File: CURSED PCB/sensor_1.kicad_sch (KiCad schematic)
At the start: 20 parts, among them J1 Programming Header, J2 Micro_SD_Card, J4 2 Wire Block for PZT, U10 MCP2562, U12 AD5761BRUZ, U3 STM32G431KBT6, Y1 24Hz crystal

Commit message: i am a LED
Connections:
- net +3.3VD: no longer JP2.2 (B)
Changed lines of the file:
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@@
-	)
-	(junction
-		(at 34.29 20.32)
-		(diameter 0)
-		(color 0 0 0 0)
 	)
 	(junction
@@
 	(wire
 		(pts
-			(xy 34.29 20.32) (xy 34.29 19.05)
-		)
-		(stroke
-			(width 0)
-			(type default)
-		)
-	)
-	(wire
-		(pts
 			(xy 66.04 74.93) (xy 85.09 74.93)
 		)
@@
 	(wire
 		(pts
-			(xy 34.29 20.32) (xy 34.29 36.83)
+			(xy 34.29 19.05) (xy 34.29 36.83)
 		)
 		(stroke
@@
 	(wire
 		(pts
-			(xy 34.29 20.32) (xy 38.1 20.32)
-		)
-		(stroke
-			(width 0)
-			(type default)
-		)
-	)
-	(wire
-		(pts
 			(xy 118.11 121.92) (xy 118.11 129.54)
 		)
@@
 		)
 		(stroke
-			(width 0)
-			(type default)
-		)
-	)
-	(wire
-		(pts
-			(xy 38.1 20.32) (xy 38.1 25.4)
-		)
-		(stroke

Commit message: tee
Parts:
- added D1: RED LED, LED_SMD:LED_0603_1608Metric_Pad1.05x0.95mm_HandSolder, symbol Device:LED
- added D3: GREEN LED, LED_SMD:LED_0603_1608Metric_Pad1.05x0.95mm_HandSolder, symbol Device:LED
- added R1, R3, R4, R5: 22R, Resistor_SMD:R_0603_1608Metric_Pad0.98x0.95mm_HandSolder, symbol Device:R_US
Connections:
- net +3.3VD: now also JP2.2 (B); no longer D2.1 (K), R2.1
- net MISO: now also R5.1; no longer J2.7 (DAT0)
- net MOSI: now also R4.1; no longer J2.3 (CMD)
- net at D2.2 (A), JP2.1 (A): now also D1.2 (A), D3.2 (A)
- net at U3.5 (PA0): now also R3.2
- net at U3.7 (PA2): now also R1.2
- new net: J2.3 (CMD), R4.2
- new net: D3.1 (K), R3.1
- new net: D1.1 (K), R1.1
- new net: D2.1 (K), R2.1
- new net: J2.7 (DAT0), R5.2
- no-connect marks 12 -> 10
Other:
- moved on the sheet: D2, JP2, R2

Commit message: wire
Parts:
- added R14: 22R, Resistor_SMD:R_0603_1608Metric_Pad0.98x0.95mm_HandSolder, symbol Device:R_US
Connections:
- net CS2: now also R14.1; no longer J2.2 (DAT3/CD)
- net MKLKIN: now also U3.21 (PA11)
- new net: J2.2 (DAT3/CD), R14.2
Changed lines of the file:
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@@
 	(wire
 		(pts
+			(xy 71.12 67.31) (xy 85.09 67.31)
+		)
+		(stroke
+			(width 0)
+			(type default)
+		)
+	)
+	(wire
+		(pts
 			(xy 30.48 25.4) (xy 46.99 25.4)
 		)
@@
 	(wire
 		(pts
-			(xy 13.97 157.48) (xy 62.23 157.48)
+			(xy 25.4 149.86) (xy 15.24 149.86)
 		)
 		(stroke
@@
 	(wire
 		(pts
+			(xy 15.24 157.48) (xy 62.23 157.48)
+		)
+		(stroke
+			(width 0)
+			(type default)
+		)
+	)
+	(wire
+		(pts
 			(xy 52.07 167.64) (xy 52.07 185.42)
 		)
@@
 	)
 	(label "MKLKIN"
-		(at 63.5 66.04 0)
+		(at 71.12 67.31 0)
 		(effects
 			(font
@@
 	)
 	(label "CS2"
-		(at 13.97 157.48 0)
+		(at 25.4 149.86 0)
 		(effects
 			(font
@@
 					(unit 1)
 				)
+			)
+		)
+	)
+	(symbol
+		(lib_id "Device:R_US")
+		(at 15.24 153.67 0)
+		(unit 1)
+		(exclude_from_sim no)
+		(in_bom yes)
+		(on_board yes)
+		(dnp no)
+		(fields_autoplaced yes)
+		(property "Reference" "R14"
+			(at 17.78 152.3999 0)
+			(effects
+				(font
+					(size 1.27 1.27)
+				)
+				(justify left)
+			)
+		)
+		(property "Value" "22R"
+			(at 17.78 154.9399 0)
+			(effects
+				(font
+					(size 1.27 1.27)
+				)
+				(justify left)
+			)
+		)
+		(property "Footprint" "Resistor_SMD:R_0603_1608Metric_Pad0.98x0.95mm_HandSolder"
+			(at 16.256 153.924 90)
+			(effects
+				(font
+					(size 1.27 1.27)
+				)
+				(hide yes)
+			)
+		)
+		(property "Datasheet" "~"
+			(at 15.24 153.67 0)
+			(effects
+				(font
+					(size 1.27 1.27)
+				)
+				(hide yes)
+			)
+		)
+		(property "Description" "Resistor, US symbol"
+			(at 15.24 153.67 0)
+			(effects
+				(font
+					(size 1.27 1.27)
+				)
+				(hide yes)
+			)
+		)
+		(pin "2"
+		)
+		(pin "1"
+		)
+		(instances
+			(project "sensor_1"
+				(path "/9fb1a86f-679c-4b88-9ed1-932f4f414580"
+					(reference "R14")
+					(unit 1)
+				)

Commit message: small error
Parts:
- R1, R2, R3: value 22R -> 220R
- R14, R4, R5: value 22R -> 10k
- Y1: value 24Hz crystal -> 24MHz crystal
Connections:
- no-connect marks 10 -> 12
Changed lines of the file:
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@@
 	)
 	(no_connect
+		(at 85.09 69.85)
+	)
+	(no_connect
+		(at 85.09 59.69)
+	)
+	(no_connect
 		(at 138.43 91.44)
 	)
@@
 			)
 		)
-		(property "Value" "22R"
+		(property "Value" "10k"
 			(at 27.94 157.4799 0)
 			(effects
@@
 			)
 		)
-		(property "Value" "22R"
+		(property "Value" "220R"
 			(at 49.53 39.3699 0)
 			(effects
@@
 			)
 		)
-		(property "Value" "22R"
+		(property "Value" "220R"
 			(at 33.02 43.1799 0)
 			(effects
@@
 			)
 		)
-		(property "Value" "24Hz crystal"
+		(property "Value" "24MHz crystal"
 			(at 218.44 138.3598 90)
 			(effects
@@
 			)
 		)
-		(property "Value" "22R"
+		(property "Value" "10k"
 			(at 46.99 173.9899 0)
 			(effects
@@
 			)
 		)
-		(property "Value" "22R"
+		(property "Value" "220R"
 			(at 17.78 44.4499 0)
 			(effects
@@
 			)
 		)
-		(property "Value" "22R"
+		(property "Value" "10k"
 			(at 17.78 154.9399 0)
 			(effects

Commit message: redone pcb
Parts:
- removed J1: Programming Header, canhw_footprints:PinSocket_5x2.54_SMD_90deg_952-3198-1-ND, symbol Connector:Conn_01x05_Socket
- added J1: Conn_02x07_Odd_Even, Connector_PinHeader_1.27mm:PinHeader_2x07_P1.27mm_Vertical_SMD, symbol Connector_Generic:Conn_02x07_Odd_Even
- C1, C2, C3, C4, C5, C6, C7: footprint Capacitor_SMD:C_0603_1608Metric_Pad1.08x0.95mm_HandSolder -> Capacitor_SMD:C_0805_2012Metric_Pad1.18x1.45mm_HandSolder
- D1, D2, D3: footprint LED_SMD:LED_0603_1608Metric_Pad1.05x0.95mm_HandSolder -> LED_SMD:LED_0805_2012Metric_Pad1.15x1.40mm_HandSolder
- R1, R14, R2, R3, R4, R5: footprint Resistor_SMD:R_0603_1608Metric_Pad0.98x0.95mm_HandSolder -> Resistor_SMD:R_0805_2012Metric_Pad1.20x1.40mm_HandSolder
- TP1, TP4, TP5: footprint TestPoint:TestPoint_Loop_D2.50mm_Drill1.0mm -> TestPoint:TestPoint_Pad_1.5x1.5mm
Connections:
- net +3.3VD: now also R14.1, R4.1, R5.1, J1.8 (Pin_8)
- net CS2: now also J2.2 (DAT3/CD), R14.2; no longer R14.1
- net GND: now also J1.10 (Pin_10); no longer C3.1, C7.2, U3.14 (VSSA)
- net MCLR: now also J1.12 (Pin_12)
- net MISO: now also J2.7 (DAT0), R5.2; no longer R5.1
- net MOSI: now also J2.3 (CMD), R4.2; no longer R4.1
- net PGC/ICSPDAT: now also J1.4 (Pin_4)
- net PGD/ICSPCLK: now also J1.6 (Pin_6)
- new net AGND: C3.1, C7.2, U3.14 (VSSA)
- no-connect marks 12 -> 21
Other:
- moved on the sheet: C1, R4, R5

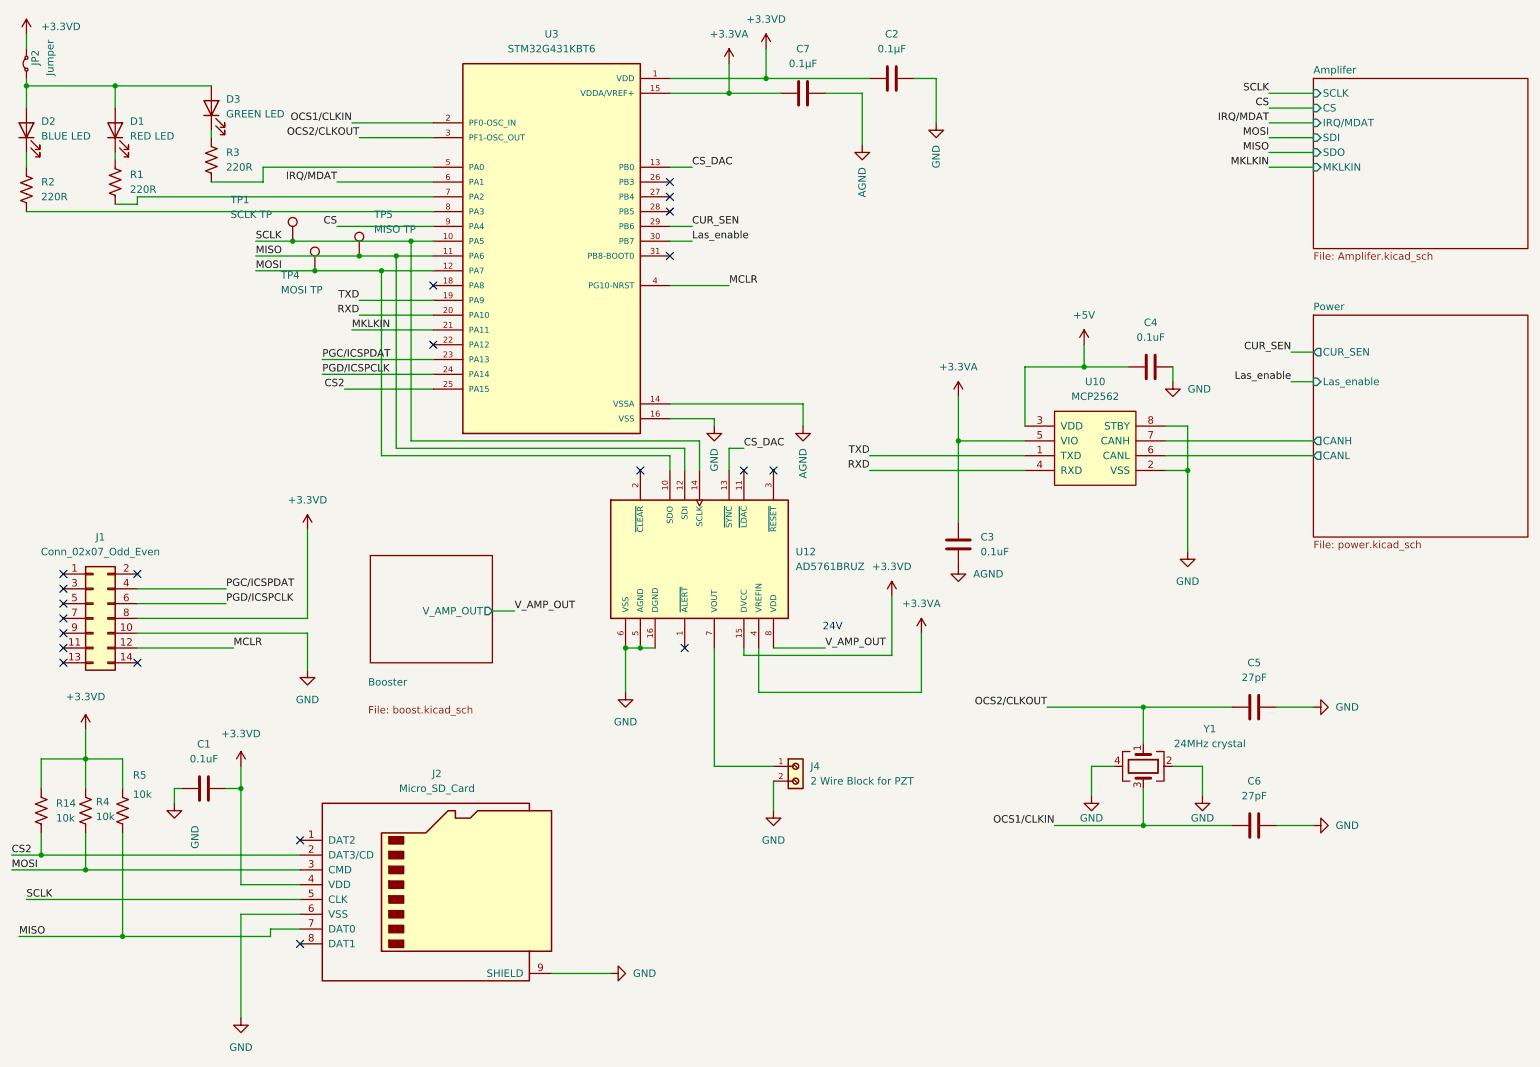
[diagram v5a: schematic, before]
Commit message: no spilt-ground plane (bad idea)
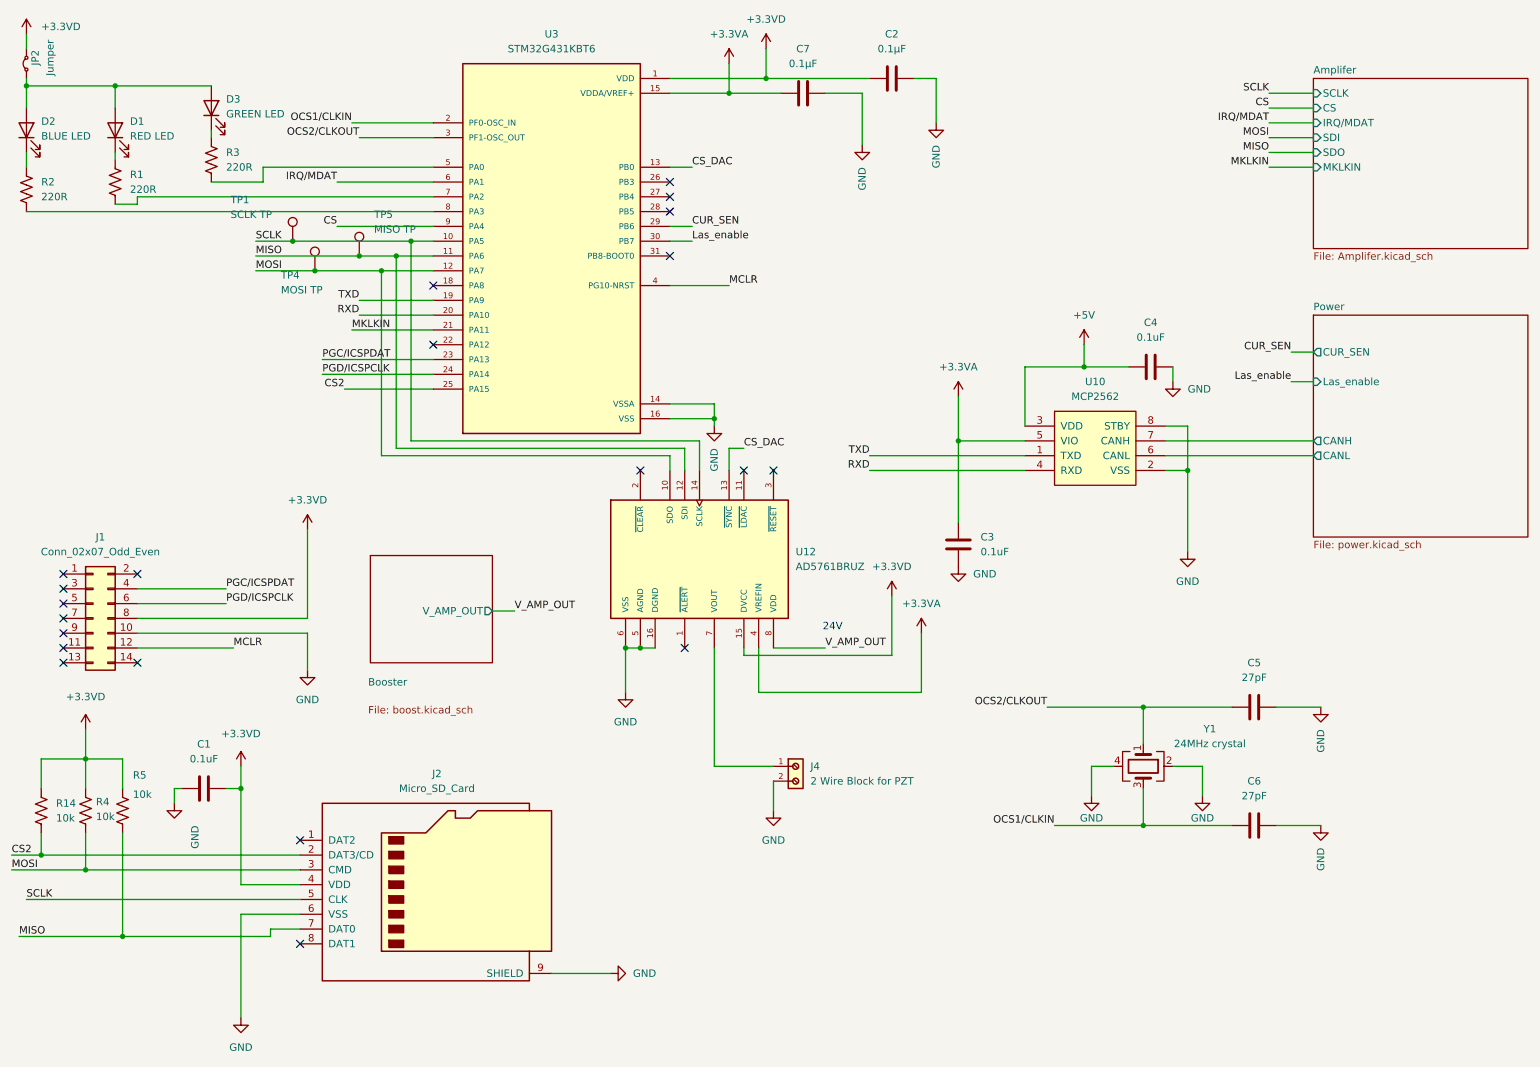
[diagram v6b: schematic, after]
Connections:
- net AGND is gone; now on net GND: C3.1, C7.2, U3.14 (VSSA)
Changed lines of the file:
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@@
 	)
 	(junction
+		(at 133.35 82.55)
+		(diameter 0)
+		(color 0 0 0 0)
+	)
+	(junction
 		(at 76.2 57.15)
 		(diameter 0)
@@
 	(wire
 		(pts
-			(xy 229.87 152.4) (xy 236.22 152.4)
+			(xy 229.87 152.4) (xy 237.49 152.4)
 		)
 		(stroke
@@
 	(wire
 		(pts
-			(xy 148.59 80.01) (xy 148.59 83.82)
+			(xy 142.24 24.13) (xy 160.02 24.13)
 		)
 		(stroke
@@
 	(wire
 		(pts
-			(xy 142.24 24.13) (xy 160.02 24.13)
+			(xy 71.12 31.75) (xy 85.09 31.75)
 		)
 		(stroke
@@
 	(wire
 		(pts
-			(xy 71.12 31.75) (xy 85.09 31.75)
+			(xy 31.75 171.45) (xy 57.15 171.45)
 		)
 		(stroke
@@
 	(wire
 		(pts
-			(xy 31.75 171.45) (xy 57.15 171.45)
+			(xy 46.99 41.91) (xy 55.88 41.91)
 		)
 		(stroke
@@
 	(wire
 		(pts
-			(xy 46.99 41.91) (xy 55.88 41.91)
+			(xy 229.87 132.08) (xy 237.49 132.08)
 		)
 		(stroke
@@
 	(wire
 		(pts
-			(xy 125.73 80.01) (xy 148.59 80.01)
-		)
-		(stroke
-			(width 0)
-			(type default)
-		)
-	)
-	(wire
-		(pts
 			(xy 15.24 24.13) (xy 15.24 25.4)
 		)
@@
 	(wire
 		(pts
-			(xy 229.87 132.08) (xy 236.22 132.08)
+			(xy 52.07 142.24) (xy 52.07 146.05)
 		)
 		(stroke
@@
 	(wire
 		(pts
-			(xy 52.07 142.24) (xy 52.07 146.05)
+			(xy 160.02 88.9) (xy 186.69 88.9)
 		)
 		(stroke
@@
 	(wire
 		(pts
-			(xy 160.02 88.9) (xy 186.69 88.9)
+			(xy 214.63 83.82) (xy 214.63 91.44)
 		)
 		(stroke
@@
 	(wire
 		(pts
-			(xy 214.63 83.82) (xy 214.63 91.44)
+			(xy 72.39 34.29) (xy 85.09 34.29)
 		)
 		(stroke
@@
 	(wire
 		(pts
-			(xy 72.39 34.29) (xy 85.09 34.29)
+			(xy 55.88 39.37) (xy 85.09 39.37)
 		)
 		(stroke
@@
 	(wire
 		(pts
-			(xy 55.88 39.37) (xy 85.09 39.37)
+			(xy 138.43 121.92) (xy 138.43 123.19)
 		)
 		(stroke
@@
 	(wire
 		(pts
-			(xy 138.43 121.92) (xy 138.43 123.19)
+			(xy 133.35 80.01) (xy 133.35 82.55)
 		)
 		(stroke
@@
 	(wire
 		(pts
+			(xy 125.73 80.01) (xy 133.35 80.01)
+		)
+		(stroke
+			(width 0)
+			(type default)
+		)
+	)
+	(wire
+		(pts
 			(xy 72.39 64.77) (xy 85.09 64.77)
 		)
@@
 	)
 	(symbol
-		(lib_id "power:GND")
-		(at 148.59 83.82 0)
-		(unit 1)
-		(exclude_from_sim no)
-		(in_bom yes)
-		(on_board yes)
-		(dnp no)
-		(property "Reference" "#PWR062"
-			(at 148.59 90.17 0)
-			(effects
-				(font
-					(size 1.27 1.27)
-				)
-				(hide yes)
-			)
-		)
-		(property "Value" "AGND"
-			(at 148.5901 87.63 90)
-			(effects
-				(font
-					(size 1.27 1.27)
-				)
-				(justify right)
-			)
-		)
-		(property "Footprint" ""
-			(at 148.59 83.82 0)
-			(effects
-				(font
-					(size 1.27 1.27)
-				)
-				(hide yes)
-			)
-		)
-		(property "Datasheet" ""
-			(at 148.59 83.82 0)
-			(effects
-				(font
-					(size 1.27 1.27)
-				)
-				(hide yes)
-			)
-		)
-		(property "Description" "Power symbol creates a global label with name \"GND\" , ground"
-			(at 148.59 83.82 0)
-			(effects
-				(font
-					(size 1.27 1.27)
-				)
-				(hide yes)
-			)
-		)
-		(pin "1"
-		)
-		(instances
-			(project "sensor_1"
-				(path "/9fb1a86f-679c-4b88-9ed1-932f4f414580"
-					(reference "#PWR062")
-					(unit 1)
-				)
-			)
-		)
-	)
-	(symbol
 		(lib_id "PCM_Capacitor_US_AKL:C_0201")
 		(at 208.28 73.66 90)
@@
 	(symbol
 		(lib_id "power:GND")
-		(at 236.22 132.08 90)
+		(at 237.49 132.08 0)
 		(unit 1)
 		(exclude_from_sim no)
@@
 		(dnp no)
 		(property "Reference" "#PWR019"
-			(at 242.57 132.08 0)
+			(at 237.49 138.43 0)
 			(effects
 				(font
@@
 		)
 		(property "Value" "GND"
-			(at 240.03 132.0799 90)
+			(at 237.4901 135.89 90)
 			(effects
 				(font
@@
 		)
 		(property "Footprint" ""
-			(at 236.22 132.08 0)
+			(at 237.49 132.08 0)
 			(effects
 				(font
@@
 		)
 		(property "Datasheet" ""
-			(at 236.22 132.08 0)
+			(at 237.49 132.08 0)
 			(effects
 				(font
@@
 		)
 		(property "Description" "Power symbol creates a global label with name \"GND\" , ground"
-			(at 236.22 132.08 0)
+			(at 237.49 132.08 0)
 			(effects
 				(font
@@
 			)
 		)
-		(property "Value" "AGND"
+		(property "Value" "GND"
 			(at 158.7501 39.37 90)
 			(effects
@@
 	(symbol
 		(lib_id "power:GND")
-		(at 236.22 152.4 90)
+		(at 237.49 152.4 0)
 		(unit 1)
 		(exclude_from_sim no)
@@
 		(dnp no)
 		(property "Reference" "#PWR020"
-			(at 242.57 152.4 0)
+			(at 237.49 158.75 0)
 			(effects
 				(font
@@
 		)
 		(property "Value" "GND"
-			(at 240.03 152.3999 90)
+			(at 237.4901 156.21 90)
 			(effects
 				(font
@@
 		)
 		(property "Footprint" ""
-			(at 236.22 152.4 0)
+			(at 237.49 152.4 0)
 			(effects
 				(font
@@
 		)
 		(property "Datasheet" ""
-			(at 236.22 152.4 0)
+			(at 237.49 152.4 0)
 			(effects
 				(font
@@
 		)
 		(property "Description" "Power symbol creates a global label with name \"GND\" , ground"
-			(at 236.22 152.4 0)
+			(at 237.49 152.4 0)
 			(effects
 				(font
@@
 			)
 		)
-		(property "Value" "AGND"
+		(property "Value" "GND"
 			(at 177.8 109.2199 0)
 			(effects

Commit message: adressing conner fixes
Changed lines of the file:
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@@
 	(wire
 		(pts
-			(xy 15.24 165.1) (xy 62.23 165.1)
+			(xy 12.7 165.1) (xy 62.23 165.1)
 		)
 		(stroke
@@
 	(wire
 		(pts
-			(xy 13.97 171.45) (xy 31.75 171.45)
+			(xy 12.7 171.45) (xy 31.75 171.45)
 		)
 		(stroke
@@
 	)
 	(label "SCLK"
-		(at 15.24 165.1 0)
+		(at 12.7 165.1 0)
 		(effects
 			(font
@@
 	)
 	(label "MISO"
-		(at 13.97 171.45 0)
-		(effects
-			(font
+		(at 12.7 171.45 0)
+		(effects
+			(font

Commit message: 3/4 revisons done from darian
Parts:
- added C24, C25, C26, C27: 10uF, Capacitor_SMD:C_0805_2012Metric_Pad1.18x1.45mm_HandSolder, symbol PCM_Capacitor_US_AKL:C_0201
- added C28, C29: 0.1µF, Capacitor_SMD:C_0805_2012Metric_Pad1.18x1.45mm_HandSolder, symbol PCM_Capacitor_US_AKL:C_0201
- C2: value 0.1µF -> 10uF
- C7: value 0.1µF -> 1uF
- D1, D2, D3: footprint LED_SMD:LED_0805_2012Metric_Pad1.15x1.40mm_HandSolder -> LED_SMD:LED_1206_3216Metric_Pad1.42x1.75mm_HandSolder
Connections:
- net +3.3VA: now also C7.2, C28.1; no longer C7.1
- net +3.3VD: now also C2.2, C24.2, C25.2, C29.2; no longer C2.1
- net GND: now also C2.1, C7.1, C24.1, C25.1, C26.1, C27.1, C28.2, C29.1; no longer C2.2, C7.2
- net V_AMP_OUT: now also C26.2, C27.2
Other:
- moved on the sheet: C2, C7
